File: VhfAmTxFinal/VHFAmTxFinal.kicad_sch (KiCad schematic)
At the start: 25 parts, among them J1 Conn_Coaxial_Small, J2 Conn_01x02, J3 Conn_Coaxial_Small, Q1 2SK3074

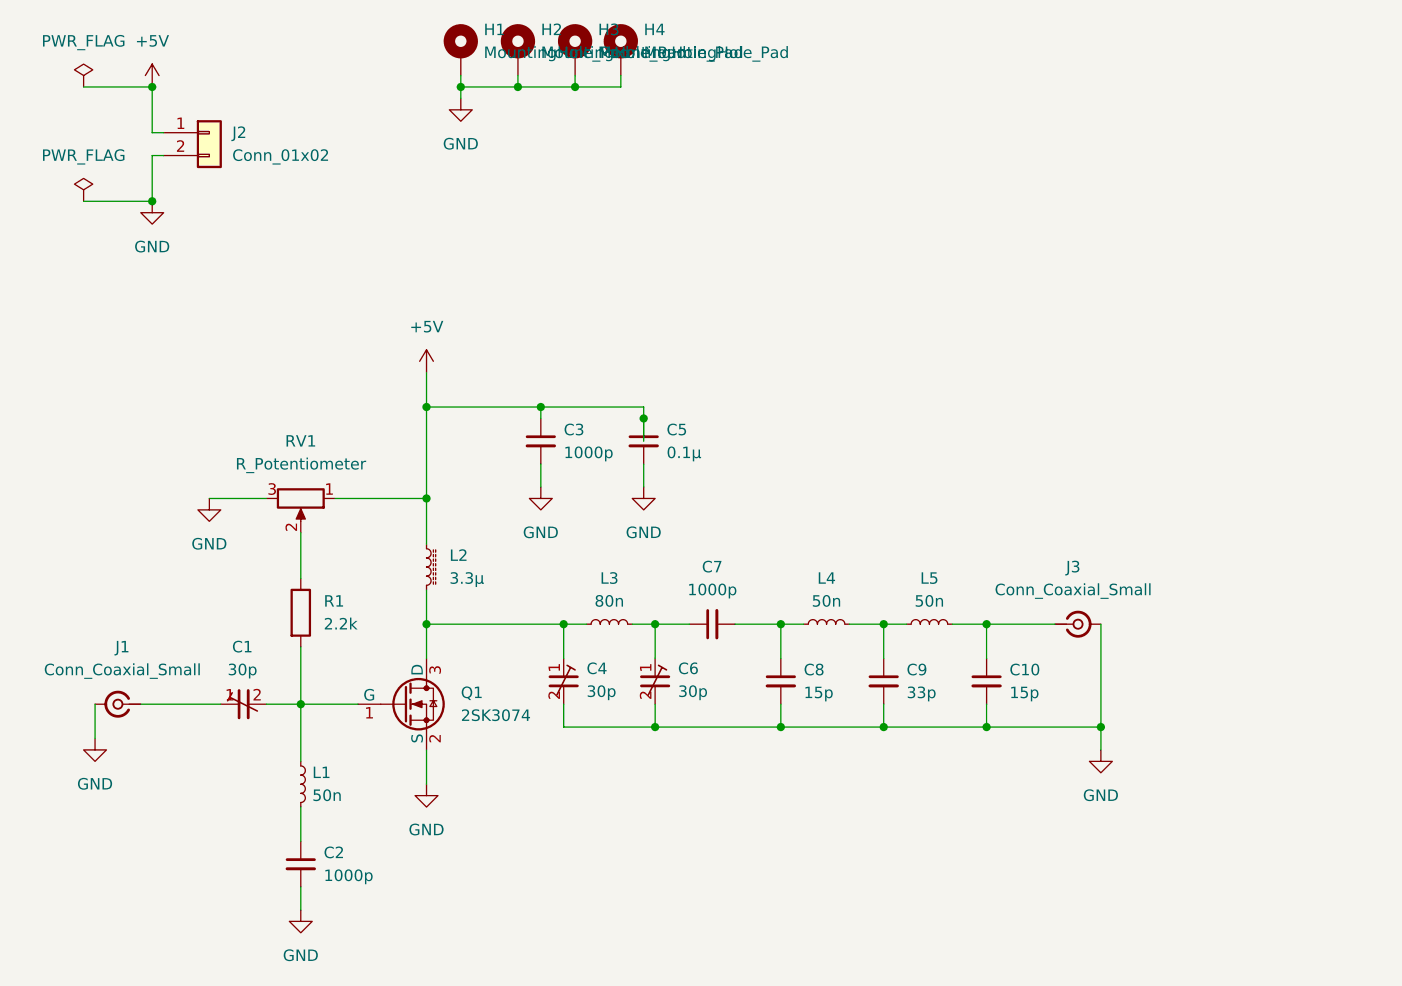
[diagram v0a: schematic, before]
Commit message: バイアス電圧用調整・安全用抵抗の追加とレイアウト修正
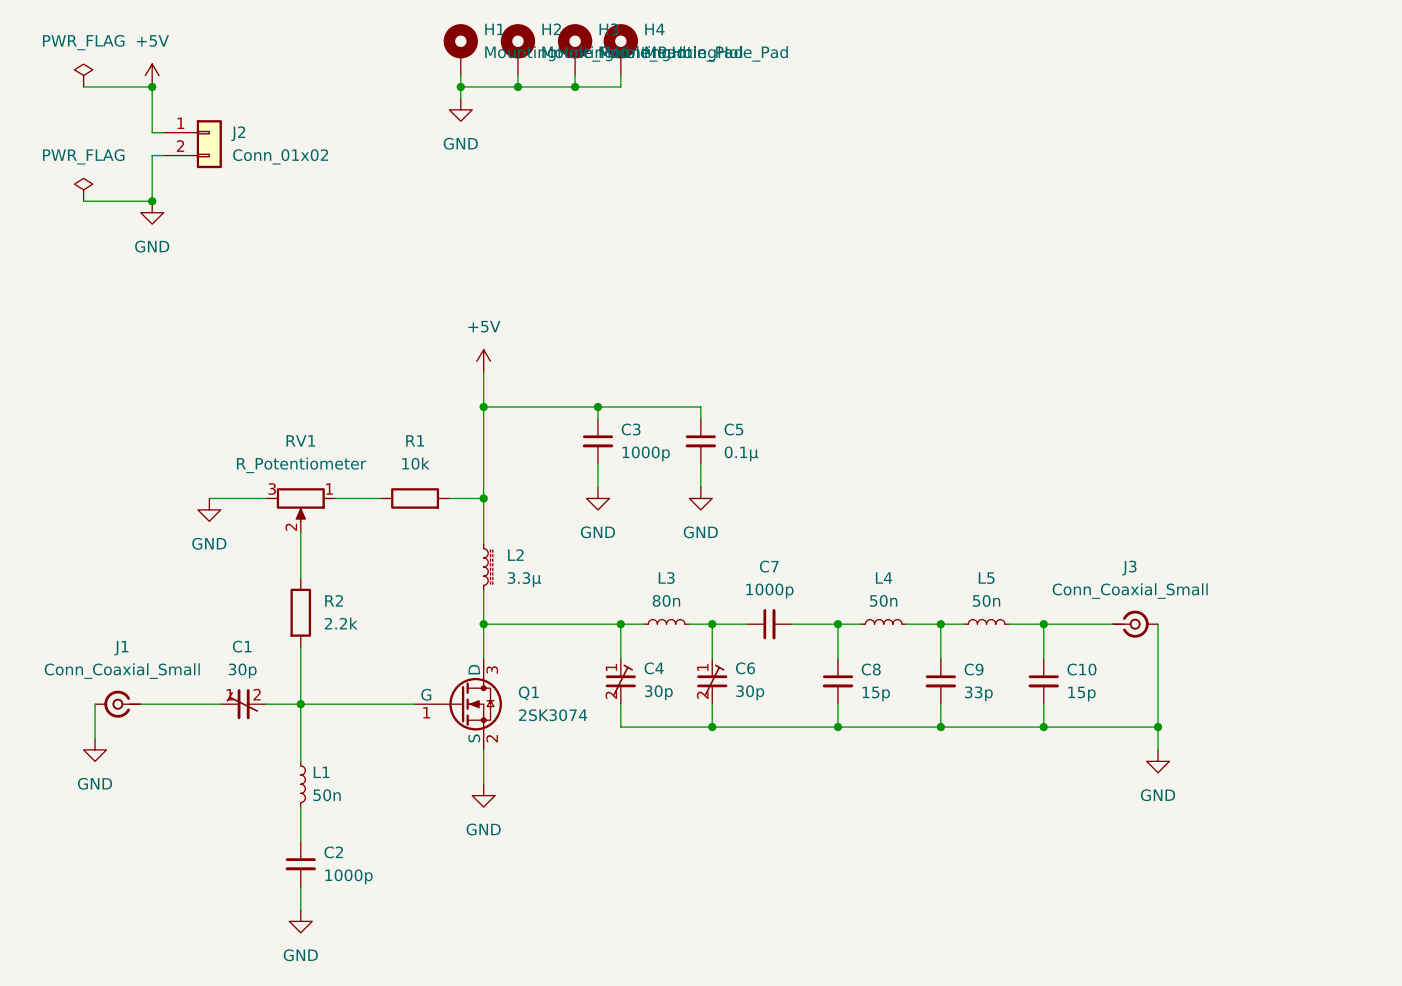
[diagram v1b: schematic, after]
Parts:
- added R1: 10k, Resistor_SMD:R_0603_1608Metric_Pad0.98x0.95mm_HandSolder, symbol Device:R
- C1, C4, C6: footprint ARPowerAmpLibrary:Ceramic_Trimmer_Capacitors_THT -> VHFAmTxFinalLibrary:Ceramic_Trimmer_Capacitors_THT
- J1, J3: footprint ARPowerAmpLibrary:SMA_S-063-49-TGG_EdgeMount_Horizontal -> VHFAmTxFinalLibrary:SMA_S-063-49-TGG_EdgeMount_Horizontal
- Q1: footprint ARPowerAmpLibrary:SOT-89-3_Handsoldering_Thirmo_Via -> VHFAmTxFinalLibrary:SOT-89-3_Handsoldering_Thirmo_Via
- renumbered R1 to R2
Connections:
- net +5V: now also R1.2; no longer RV1.1
- new net: R1.1, RV1.1
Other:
- moved on the sheet: C10, C3, C4, C5, C6, C7, C8, C9, J3, L2, L3, L4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

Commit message: HTL7G06S006Pの対応 READMEアップデート
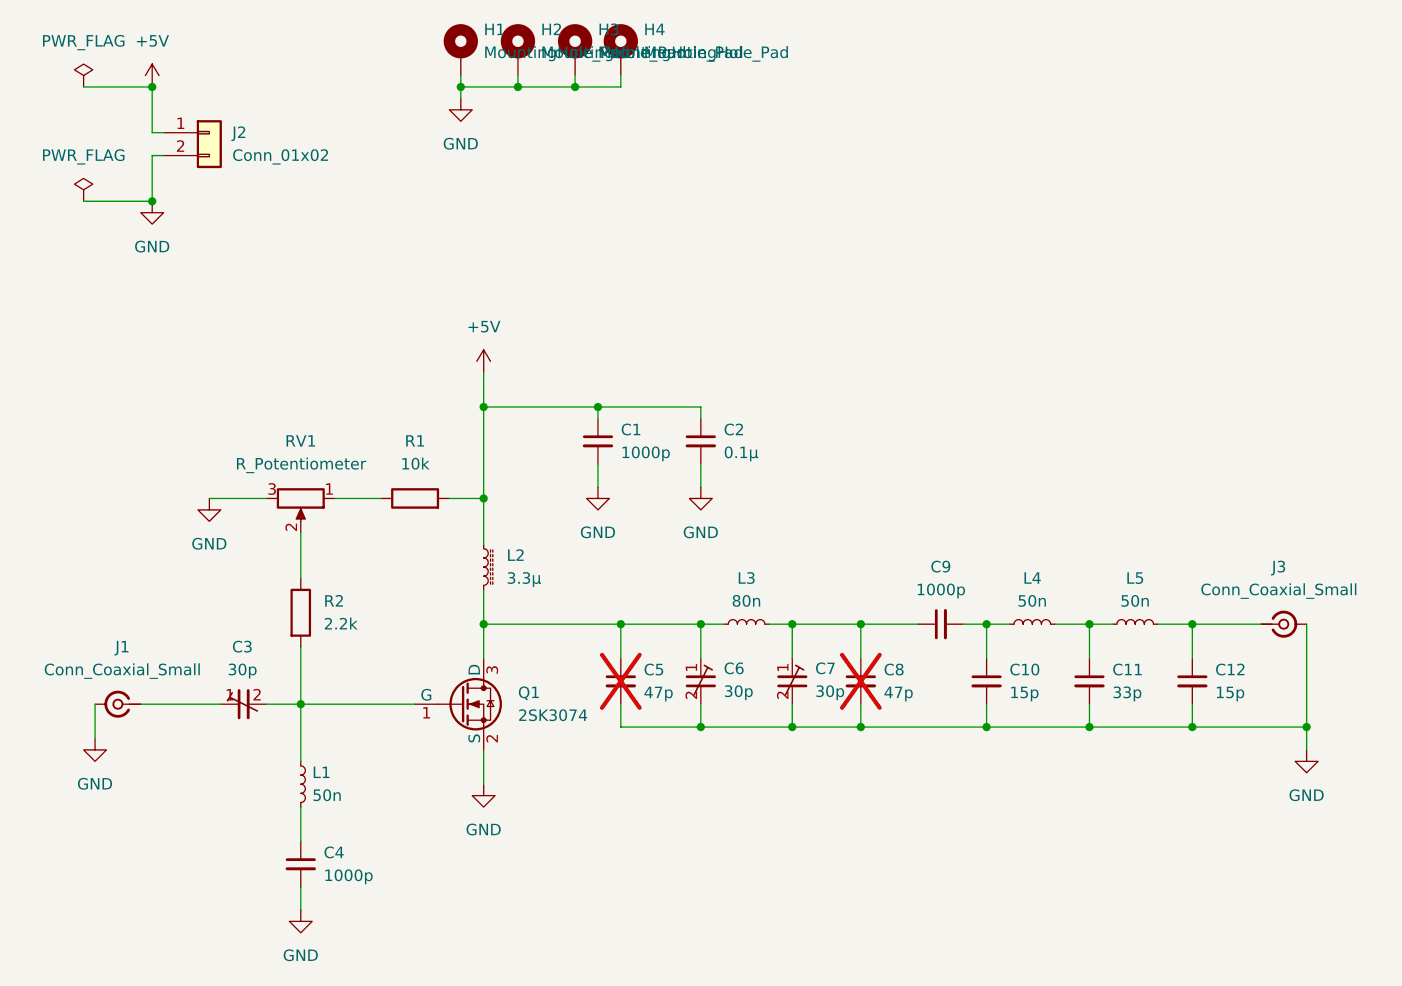
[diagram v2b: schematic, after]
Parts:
- added C5, C8: 47p, Capacitor_SMD:C_0603_1608Metric_Pad1.08x0.95mm_HandSolder, symbol Device:C_Small
- renumbered C3 to C1, C8 to C10, C9 to C11, C10 to C12, C5 to C2, C1 to C3, C2 to C4, C4 to C6, C6 to C7, C7 to C9
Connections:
- net GND: now also C5.2, C8.2
- net at C6.1, L2.2, L3.1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: now also C5.1
- net at C7.1, C9.1, L3.2: now also C8.1
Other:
- moved on the sheet: C10, C11, C12, C6, C7, C9, J3, L3, L4, L5

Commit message: 基板のレイアウト修正 v0.3
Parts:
- L1, L3, L4, L5: footprint Inductor_SMD:L_Cenker_CKCS8060 -> VHFAmTxFinalLibrary:Air_Core_Inductor_8mm
- L2: footprint Inductor_SMD:L_10.4x10.4_H4.8 -> VHFAmTxFinalLibrary:Choke_Inductor_10mm
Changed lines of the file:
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@@
 			)
 		)
-		(property "Footprint" "Inductor_SMD:L_Cenker_CKCS8060"
+		(property "Footprint" "VHFAmTxFinalLibrary:Air_Core_Inductor_8mm"
 			(at 143.51 86.36 0)
 			(effects
@@
 			)
 		)
-		(property "Footprint" "Inductor_SMD:L_Cenker_CKCS8060"
+		(property "Footprint" "VHFAmTxFinalLibrary:Air_Core_Inductor_8mm"
 			(at 100.33 86.36 0)
 			(effects
@@
 			)
 		)
-		(property "Footprint" "Inductor_SMD:L_Cenker_CKCS8060"
+		(property "Footprint" "VHFAmTxFinalLibrary:Air_Core_Inductor_8mm"
 			(at 50.8 104.14 0)
 			(effects
@@
 			)
 		)
-		(property "Footprint" "Inductor_SMD:L_Cenker_CKCS8060"
+		(property "Footprint" "VHFAmTxFinalLibrary:Air_Core_Inductor_8mm"
 			(at 132.08 86.36 0)
 			(effects
@@
 			)
 		)
-		(property "Footprint" "Inductor_SMD:L_10.4x10.4_H4.8"
+		(property "Footprint" "VHFAmTxFinalLibrary:Choke_Inductor_10mm"
 			(at 71.12 80.01 0)
 			(effects

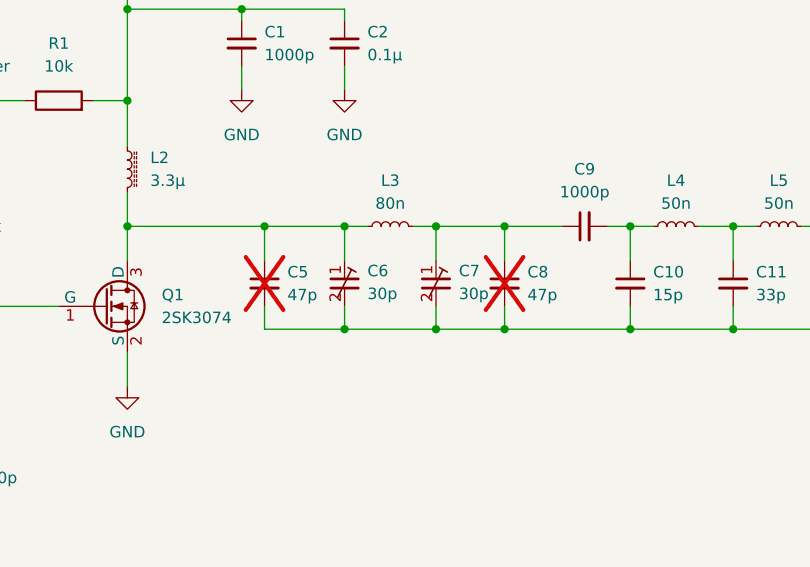
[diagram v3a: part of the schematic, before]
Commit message: ドキュメント修正ドライブ段を追加
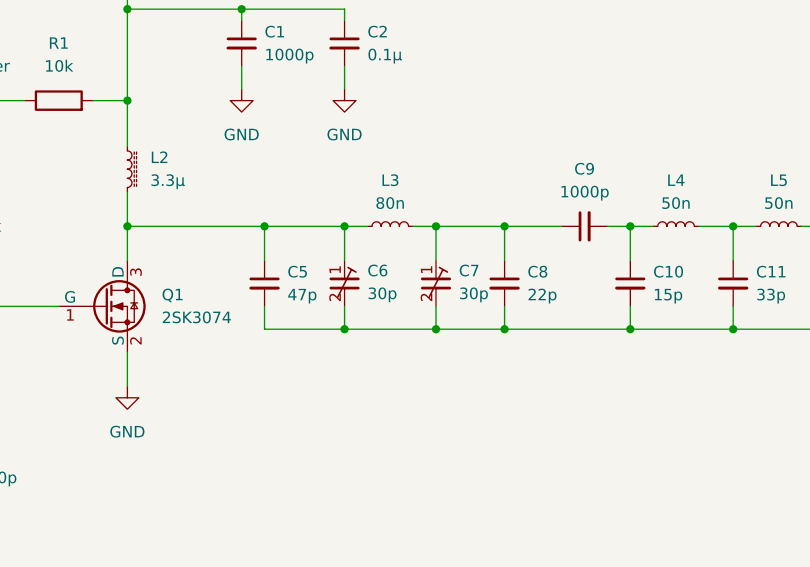
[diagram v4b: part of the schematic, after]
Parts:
- C5: now fitted
- C8: value 47p -> 22p; now fitted
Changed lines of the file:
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@@
 		(in_bom yes)
 		(on_board yes)
-		(dnp yes)
+		(dnp no)
 		(fields_autoplaced yes)
 		(property "Reference" "C8"
@@
 			)
 		)
-		(property "Value" "47p"
+		(property "Value" "22p"
 			(at 115.57 93.9862 0)
 			(effects
@@
 		(in_bom yes)
 		(on_board yes)
-		(dnp yes)
+		(dnp no)
 		(fields_autoplaced yes)
 		(property "Reference" "C5"

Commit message: 基板修正
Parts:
- Q1: footprint VHFAmTxFinalLibrary:SOT-89-3_Handsoldering_Thirmo_Via -> Package_TO_SOT_SMD:SOT-89-3_Handsoldering
- RV1: footprint Potentiometer_THT:Potentiometer_Piher_PT-10-V05_Vertical -> Potentiometer_THT:Potentiometer_Vishay_T73YP_Vertical
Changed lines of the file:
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@@
 			)
 		)
-		(property "Footprint" "Potentiometer_THT:Potentiometer_Piher_PT-10-V05_Vertical"
+		(property "Footprint" "Potentiometer_THT:Potentiometer_Vishay_T73YP_Vertical"
 			(at 50.8 72.39 0)
 			(effects
@@
 			)
 		)
-		(property "Footprint" "VHFAmTxFinalLibrary:SOT-89-3_Handsoldering_Thirmo_Via"
+		(property "Footprint" "Package_TO_SOT_SMD:SOT-89-3_Handsoldering"
 			(at 73.66 92.71 0)
 			(effects
